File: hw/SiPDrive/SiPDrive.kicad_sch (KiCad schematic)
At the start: 66 parts, among them Q1 CMSA015N06, Q2 CMSA015N06, Q3 CMSA015N06, Q4 CMSA015N06, Q5 CMSA015N06, Q6 CMSA015N06, U1 STSPIN32G4, U2 MT6701, U3 TCAN1057, U4 LDO, U5 SH-3P

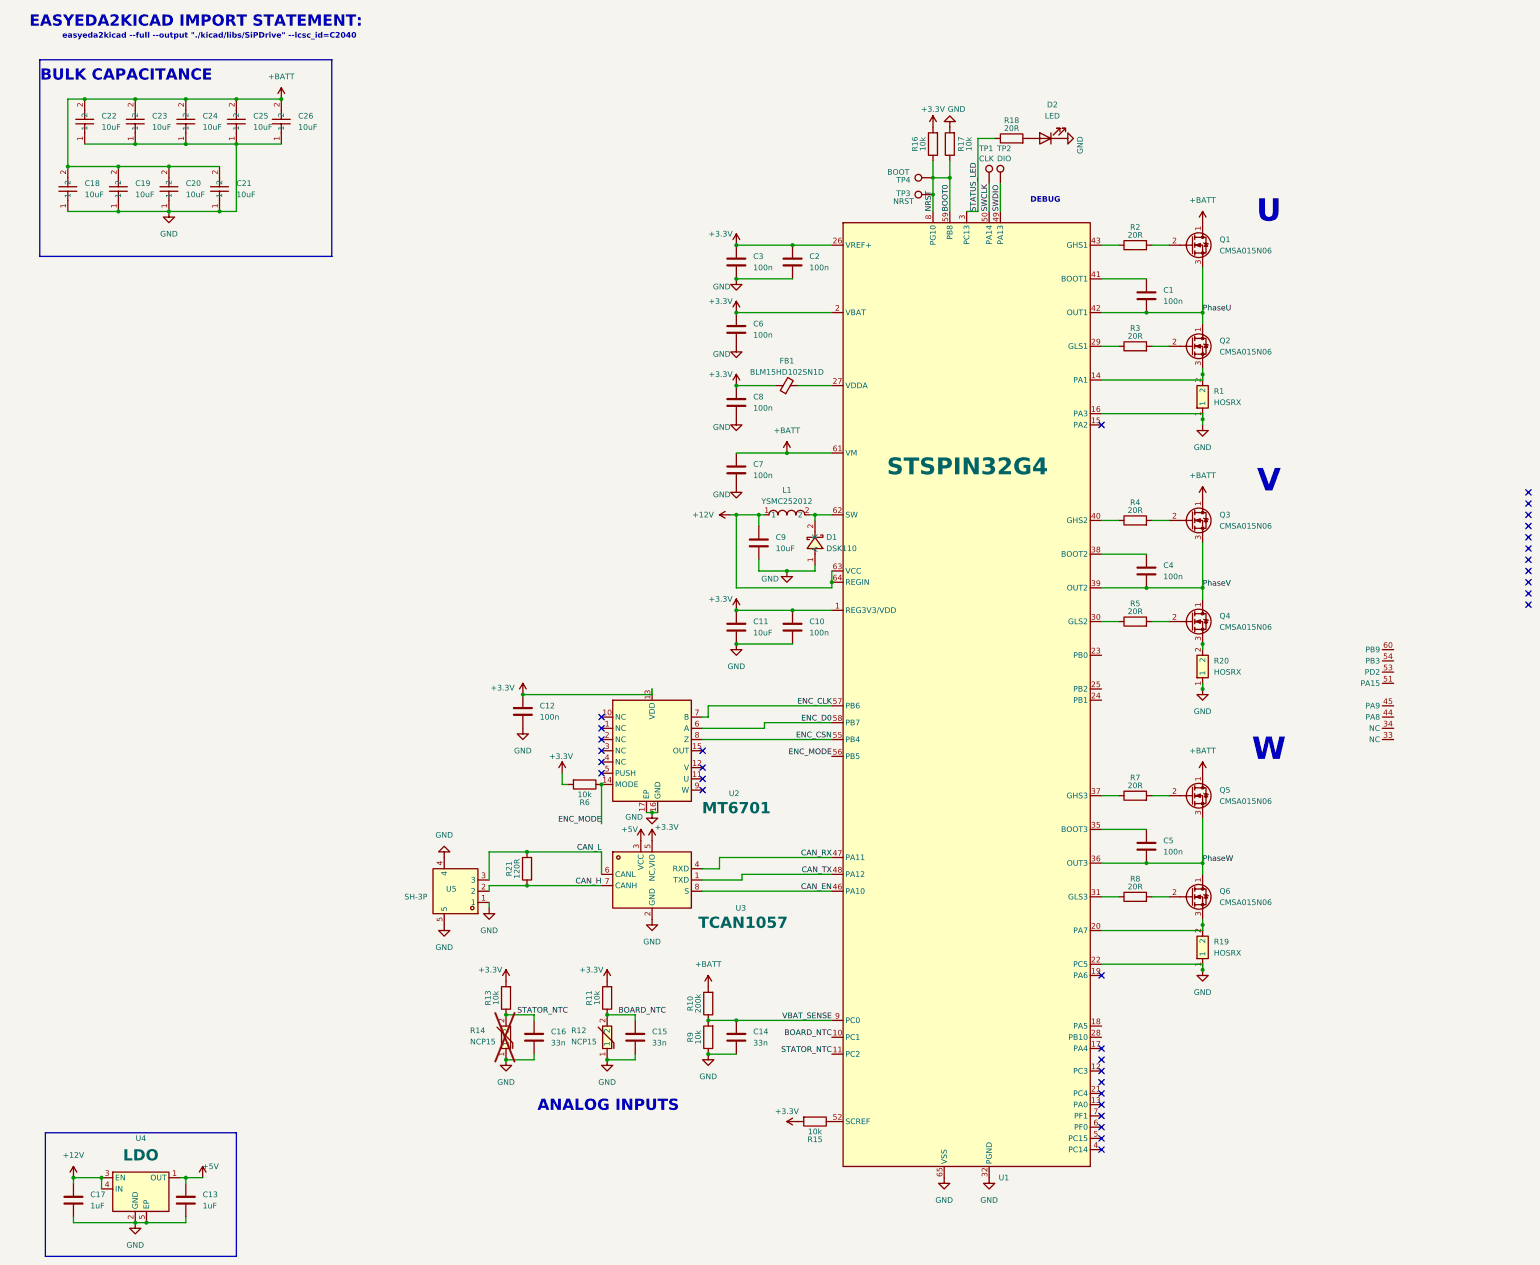
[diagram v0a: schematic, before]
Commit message: Prepare repository for GitHub release
- Add CC BY-NC 4.0 license (non-commercial use)
- Consolidate all docs (BUILD_NOTES, FW_COMPARISON_REPORT, CLAUDE,
  SCHEMATIC_REWORK) into single README with collapsible sections
- Remove legacy move_moteus.py (parent repo artifact)
- Gitignore 37MB STM32G4 reference manual (download link in README)
- Gitignore KiCad lock files
- Add EVLSPIN32G4-ACT eval board datasheet
- Update KiCad schematic and netlist (3-shunt rework in progress)
- Slim CLAUDE.md to index pointing at README

Co-Authored-By: Claude Opus 4.6 <noreply@anthropic.com>
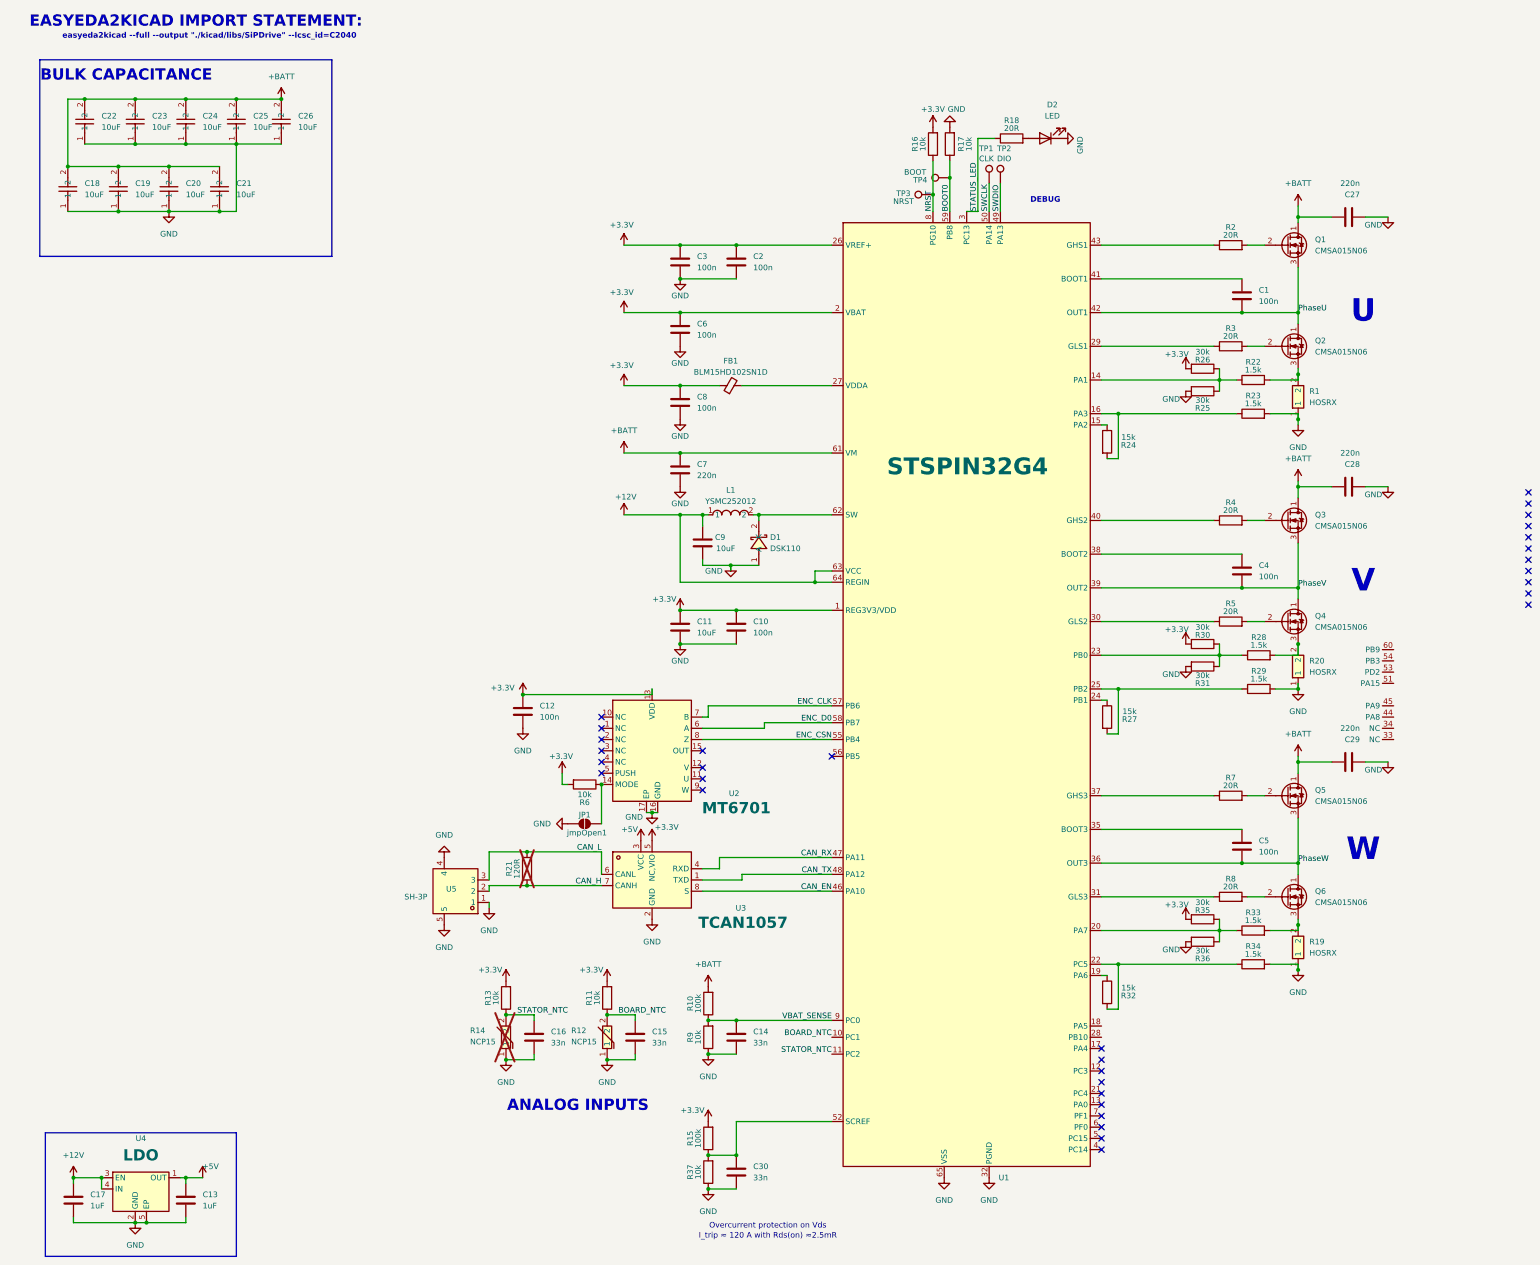
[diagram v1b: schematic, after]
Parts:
- added C27, C28, C29: 220n, Capacitor_SMD:C_0603_1608Metric, symbol Device:C
- added C30: 33n, Capacitor_SMD:C_0402_1005Metric, symbol Device:C
- added JP1: jmpOpen1, symbol Jumper:SolderJumper_2_Open
- added R22, R23, R28, R29, R33, R34: 1.5k, Resistor_SMD:R_0402_1005Metric, symbol Device:R
- added R24, R27, R32: 15k, Resistor_SMD:R_0402_1005Metric, symbol Device:R
- added R25, R26, R30, R31, R35, R36: 30k, Resistor_SMD:R_0402_1005Metric, symbol Device:R
- added R37: 10k, Resistor_SMD:R_0402_1005Metric, symbol Device:R
- C7: value 100n -> 220n; footprint Capacitor_SMD:C_0402_1005Metric -> Capacitor_SMD:C_0603_1608Metric
- R10: value 200k -> 100k
- R15: value 10k -> 100k; LCSC C60490 -> C114763
- R21: now not fitted
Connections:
- net +3.3V: now also R26.2, R30.2, R35.2
- net +BATT: now also C27.1, C28.1, C29.1
- net BOOT0: no longer R16.1, TP3.1, U1.8 (PG10)
- net GND: now also C27.2, C28.2, C29.2, C30.2, JP1.1 (A), R23.2, R25.2, R29.2, R31.2, R34.2, R36.2, R37.1; no longer U1.16 (PA3), U1.22 (PC5)
- net at Q4.3 (S), R20.2: now also R28.2
- net at Q2.3 (S), R1.2: now also R22.2; no longer U1.14 (PA1)
- net at Q6.3 (S), R19.2: now also R33.2; no longer U1.20 (PA7)
- net at R15.1, U1.52 (SCREF): now also C30.1, R37.2
- net at U1.15 (PA2): now also R24.1
- net at U1.19 (PA6): now also R32.1
- net at U1.23 (PB0): now also R28.1, R30.1, R31.1
- net at U1.24 (PB1): now also R27.1
- net at U1.25 (PB2): now also R27.2, R29.1
- net ENC_MODE: no longer names the net of R6.1, U2.14 (MODE)
- net ENC_MODE: now also JP1.2 (B); no longer U1.56 (PB5)
- new net: R32.2, R34.1, U1.22 (PC5)
- new net: R22.1, R25.1, R26.1, U1.14 (PA1)
- new net: R33.1, R35.1, R36.1, U1.20 (PA7)
- new net: R23.1, R24.2, U1.16 (PA3)
- new net NRST: R16.1, TP3.1, U1.8 (PG10)
- no-connect marks 33 -> 32
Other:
- note added: "I_trip ≈ 120 A with Rds(on) ≈2.5mR"
- note added: "Overcurrent protection on Vds"
- moved on the sheet: C1, C10, C11, C2, C3, C4, C5, C6, C7, C8, C9, D1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
